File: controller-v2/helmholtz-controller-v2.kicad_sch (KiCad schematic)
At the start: 60 parts, among them J1 Screw_Terminal_01x02, J2 Screw_Terminal_01x02, J3 Screw_Terminal_01x02, J4 Screw_Terminal_01x02, J5 Conn_01x04, U1 BDS63150AFM, U2 BDS63150AFM, U3 INA226, U4 INA226, U5 BDS63150AFM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

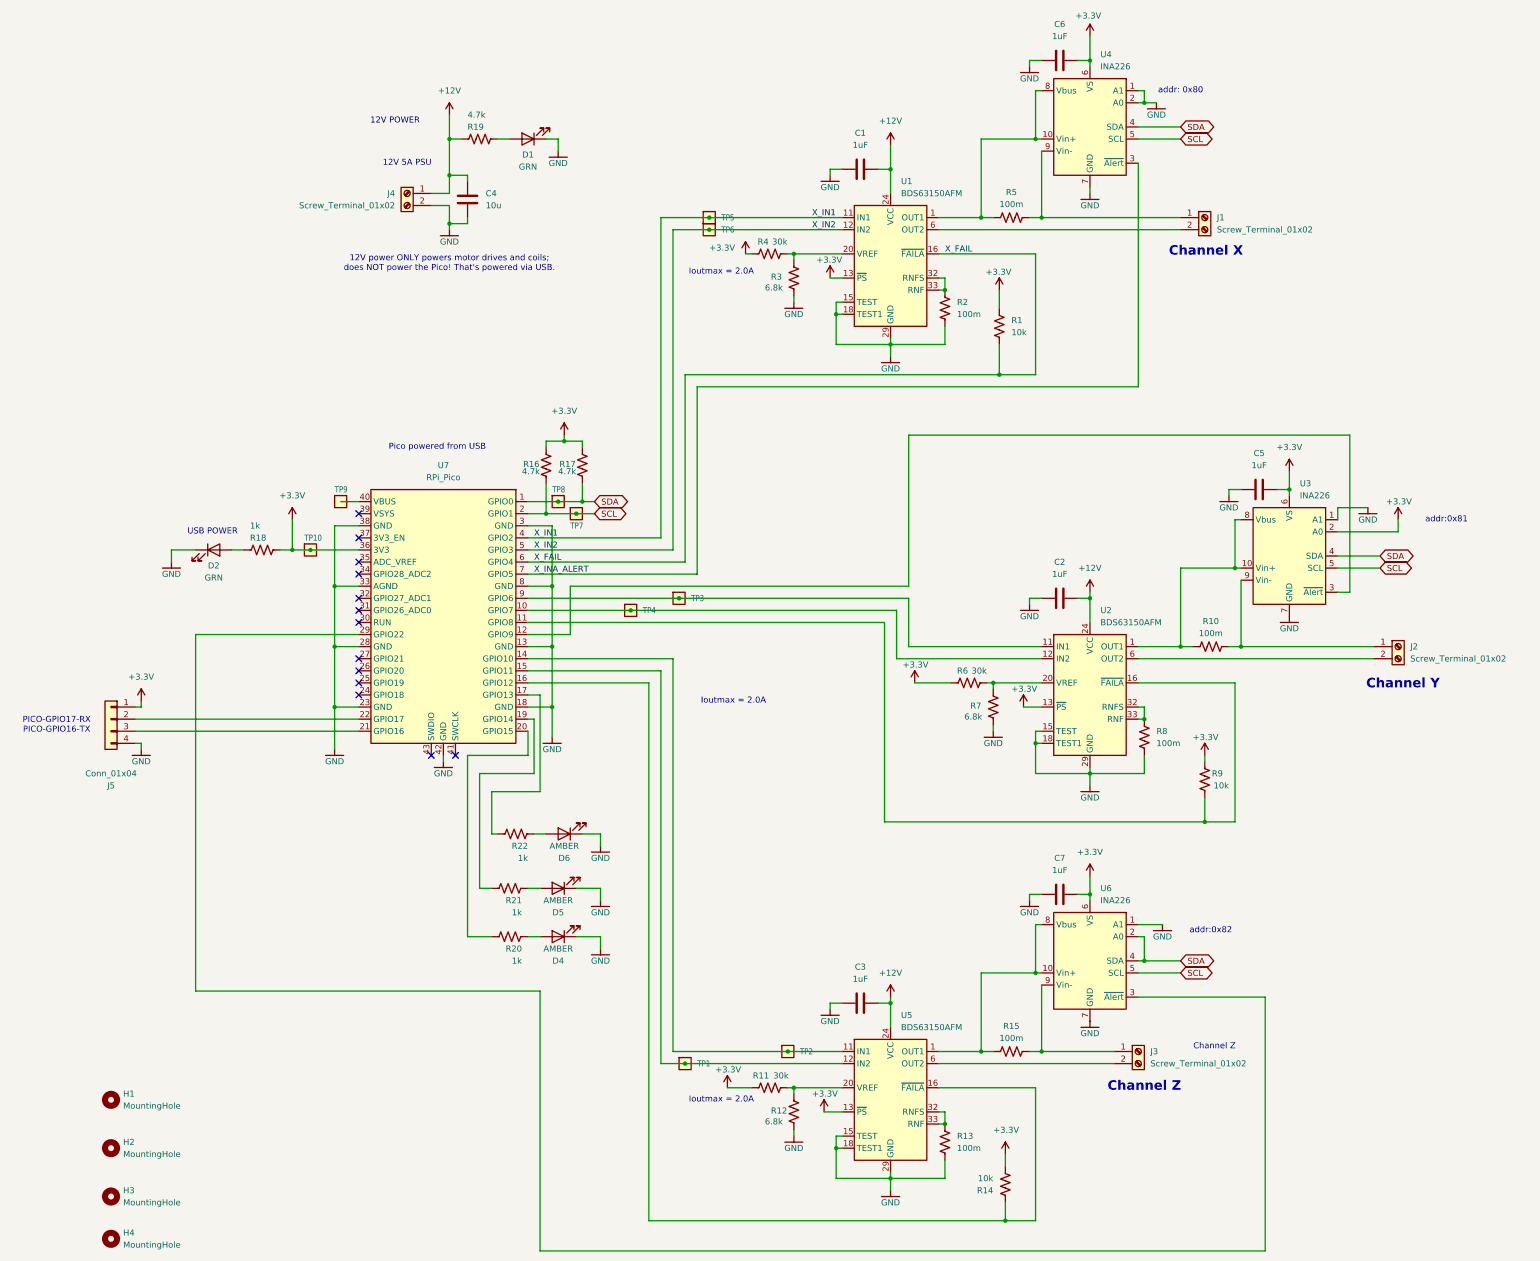
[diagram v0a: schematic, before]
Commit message: Final cleanup of board before fab.
Did some polishing on layout for better power flow.
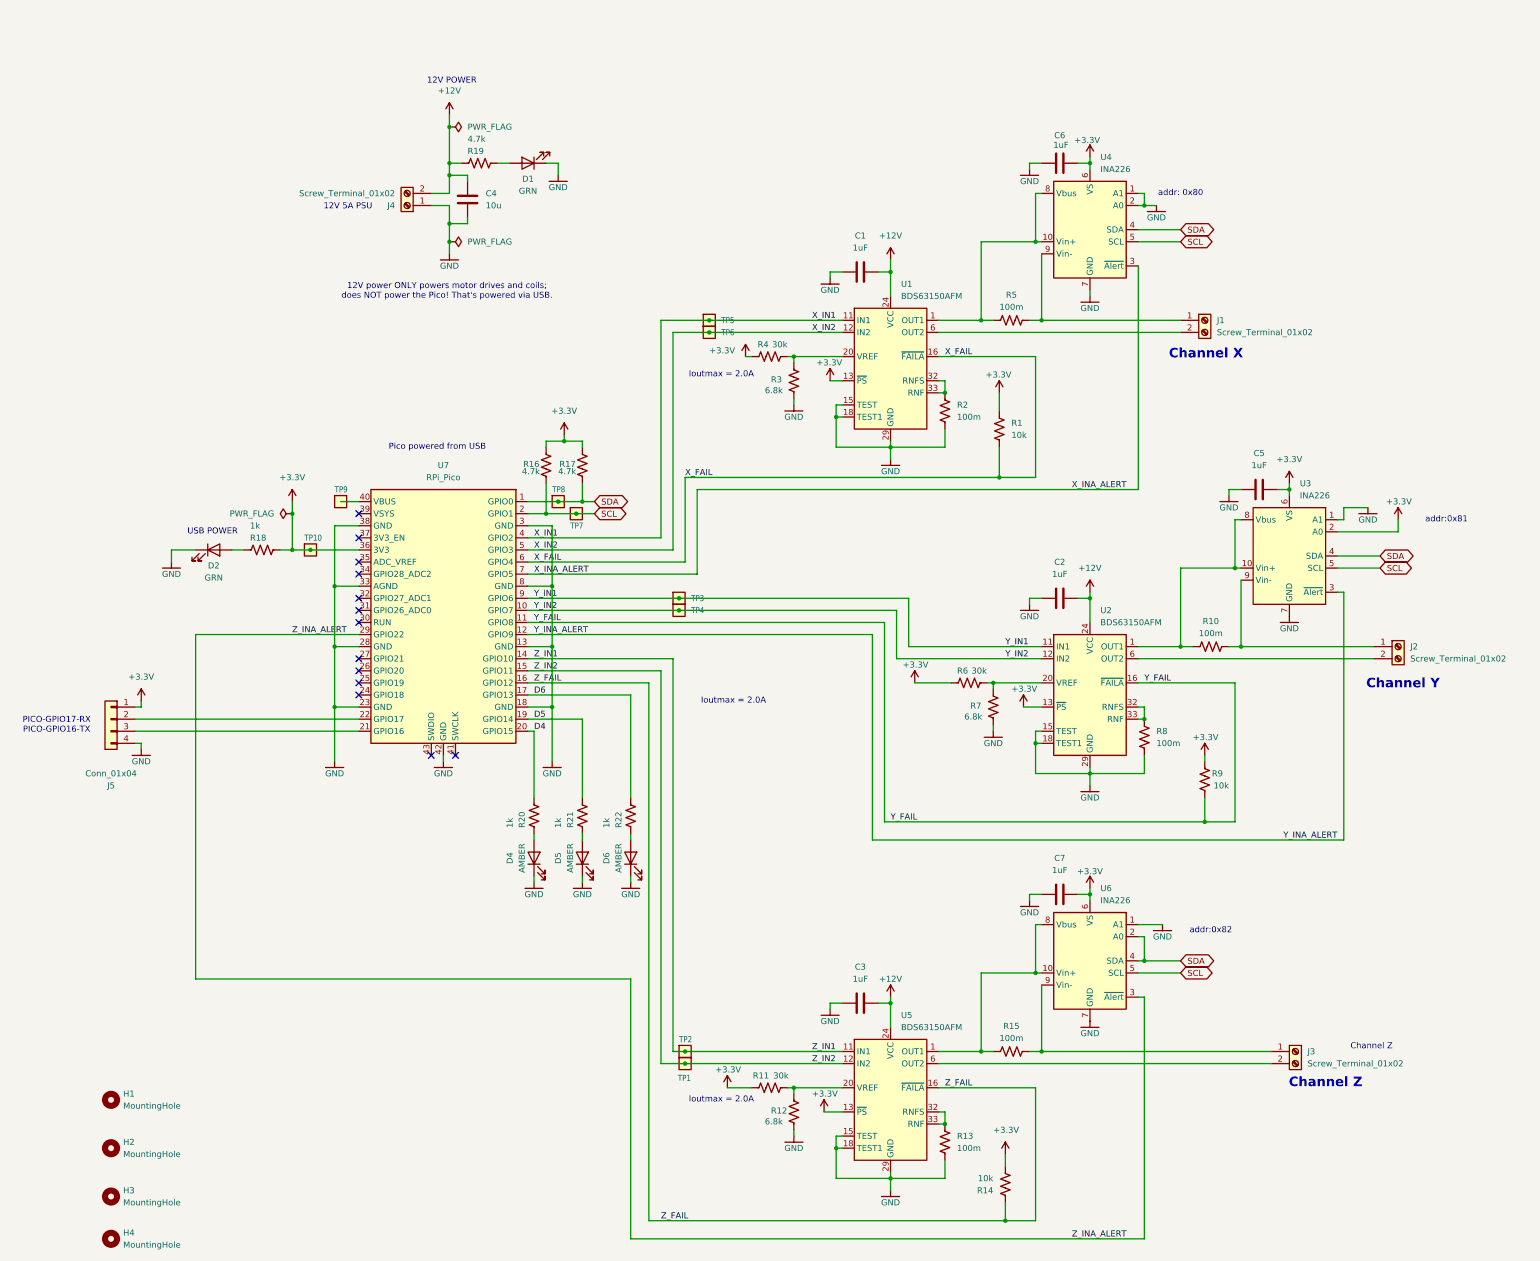
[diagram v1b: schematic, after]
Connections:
- net +12V: now also J4.2 (Pin_2); no longer J4.1 (Pin_1)
- net GND: now also J4.1 (Pin_1); no longer J4.2 (Pin_2)
- net Y_IN2: now reaches TP4.1, U2.12 (IN2), U7.10 (GPIO7)
- net Y_FAIL: now reaches R9.1, U2.16 (~{FAILA}), U7.11 (GPIO8)
- net Y_INA_ALERT: now reaches U3.3 (~{Alert}), U7.12 (GPIO9)
- net Z_IN1: now reaches TP2.1, U5.11 (IN1), U7.14 (GPIO10)
- net Z_IN2: now reaches TP1.1, U5.12 (IN2), U7.15 (GPIO11)
- net Z_FAIL: now reaches R14.1, U5.16 (~{FAILA}), U7.16 (GPIO12)
- net D6: now reaches R22.2, U7.17 (GPIO13)
- net D5: now reaches R21.2, U7.19 (GPIO14)
- net D4: now reaches R20.2, U7.20 (GPIO15)
- net Z_INA_ALERT: now reaches U6.3 (~{Alert}), U7.29 (GPIO22)
- net Y_IN1: now reaches TP3.1, U2.11 (IN1), U7.9 (GPIO6)
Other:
- moved on the sheet: C1, C6, D1, D4, D5, D6, J1, J3, J4, R1, R19, R2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

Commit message: Minor changes that bring the version to 2.1.
The 2.0 board is fabbed, and we found a few minor issues (wrong address listed in the schematic, no XYZ marking at pheonix connectors, etc).
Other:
- note added: "addr: 0x40"
- note added: "addr:0x41"
- note added: "addr:0x42"
- note removed: "addr: 0x80"
- note removed: "addr:0x81"
- note removed: "addr:0x82"
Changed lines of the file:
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@@
 	(title_block
 		(title "Helmholtz Cage Controller")
-		(date "2025-10-20")
-		(rev "2.0")
+		(date "2025-12-18")
+		(rev "2.1")
 		(company "Portland State Aerospace Society")
 	)
@@
 		)
 	)
-	(text "addr:0x82"
+	(text "addr:0x42"
 		(exclude_from_sim no)
 		(at 289.56 195.58 0)
@@
 		)
 	)
-	(text "addr: 0x80\n"
+	(text "addr: 0x40\n"
 		(exclude_from_sim no)
 		(at 283.21 40.64 0)
@@
 		)
 	)
-	(text "addr:0x81\n"
+	(text "addr:0x41\n"
 		(exclude_from_sim no)
 		(at 339.09 109.22 0)
